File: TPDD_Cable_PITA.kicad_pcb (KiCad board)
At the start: 2 copper layers, 34.6 x 10.1 mm, 5 parts, among them J1 7 x wire pads, J2 DB25_Male, Q1 DTA114EKA, Q2 DTA114EKA, Q3 DTA114EKA

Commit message: pcbway limits, readme
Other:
- net class Default: clearance 0.16 -> 0.2; trace_width 0.16 -> 0.2; via_dia 0.42 -> 0.5; via_drill 0.26 -> 0.3
- rule trace_clearance: 0.16 -> 0.2
- rule trace_min: 0.16 -> 0.2
- rule via_min_drill: 0.26 -> 0.3
- rule via_min_size: 0.42 -> 0.5

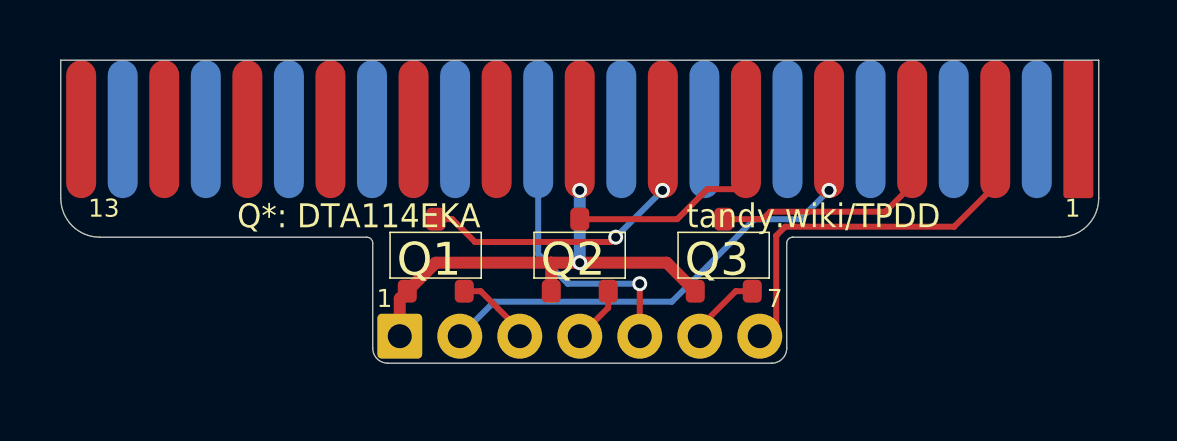
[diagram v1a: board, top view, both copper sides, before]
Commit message: kicad 6, ground zones
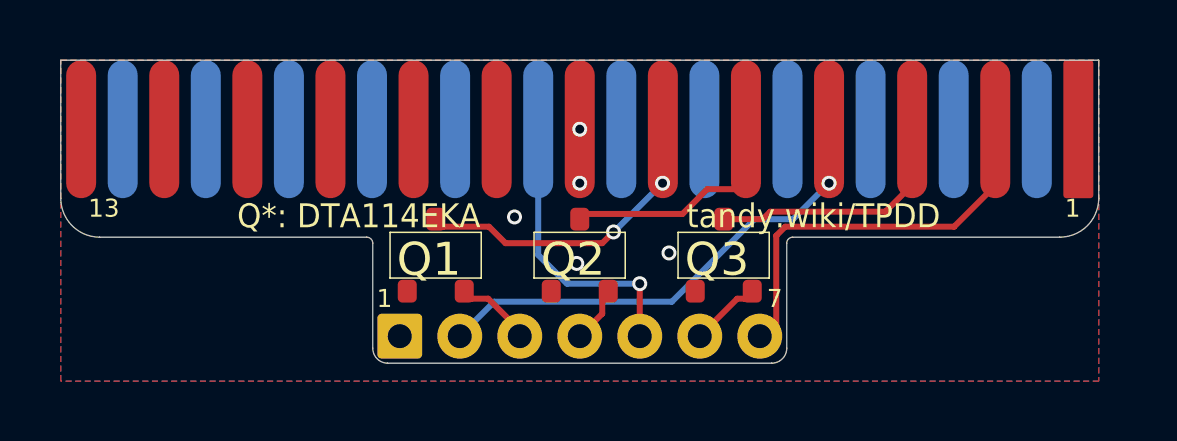
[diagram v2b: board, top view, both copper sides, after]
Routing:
- net /GND: track 15.4 -> 0.00 mm, vias 2 -> 5
- added copper zone on B.Cu, net /GND
- added copper zone on F.Cu, net /GND
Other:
- net class Default removed
